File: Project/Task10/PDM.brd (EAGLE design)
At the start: 100 x 80 mm, 43 parts

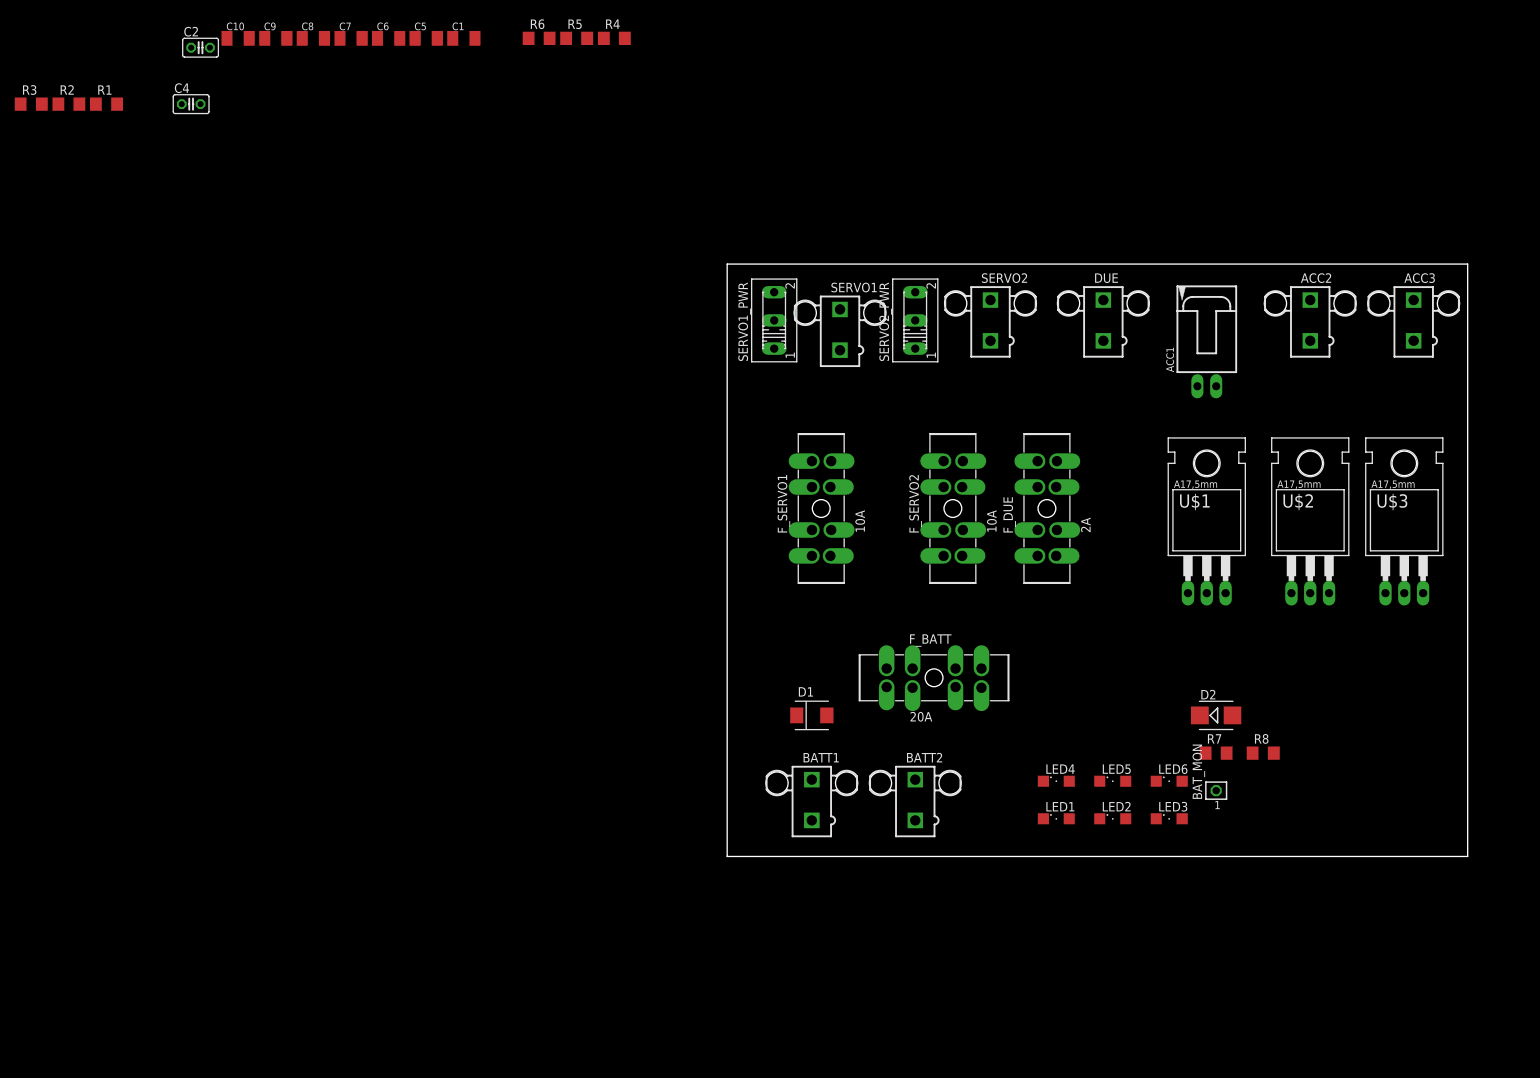
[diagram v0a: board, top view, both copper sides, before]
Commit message: Datahseet for XT60 for battery connector added
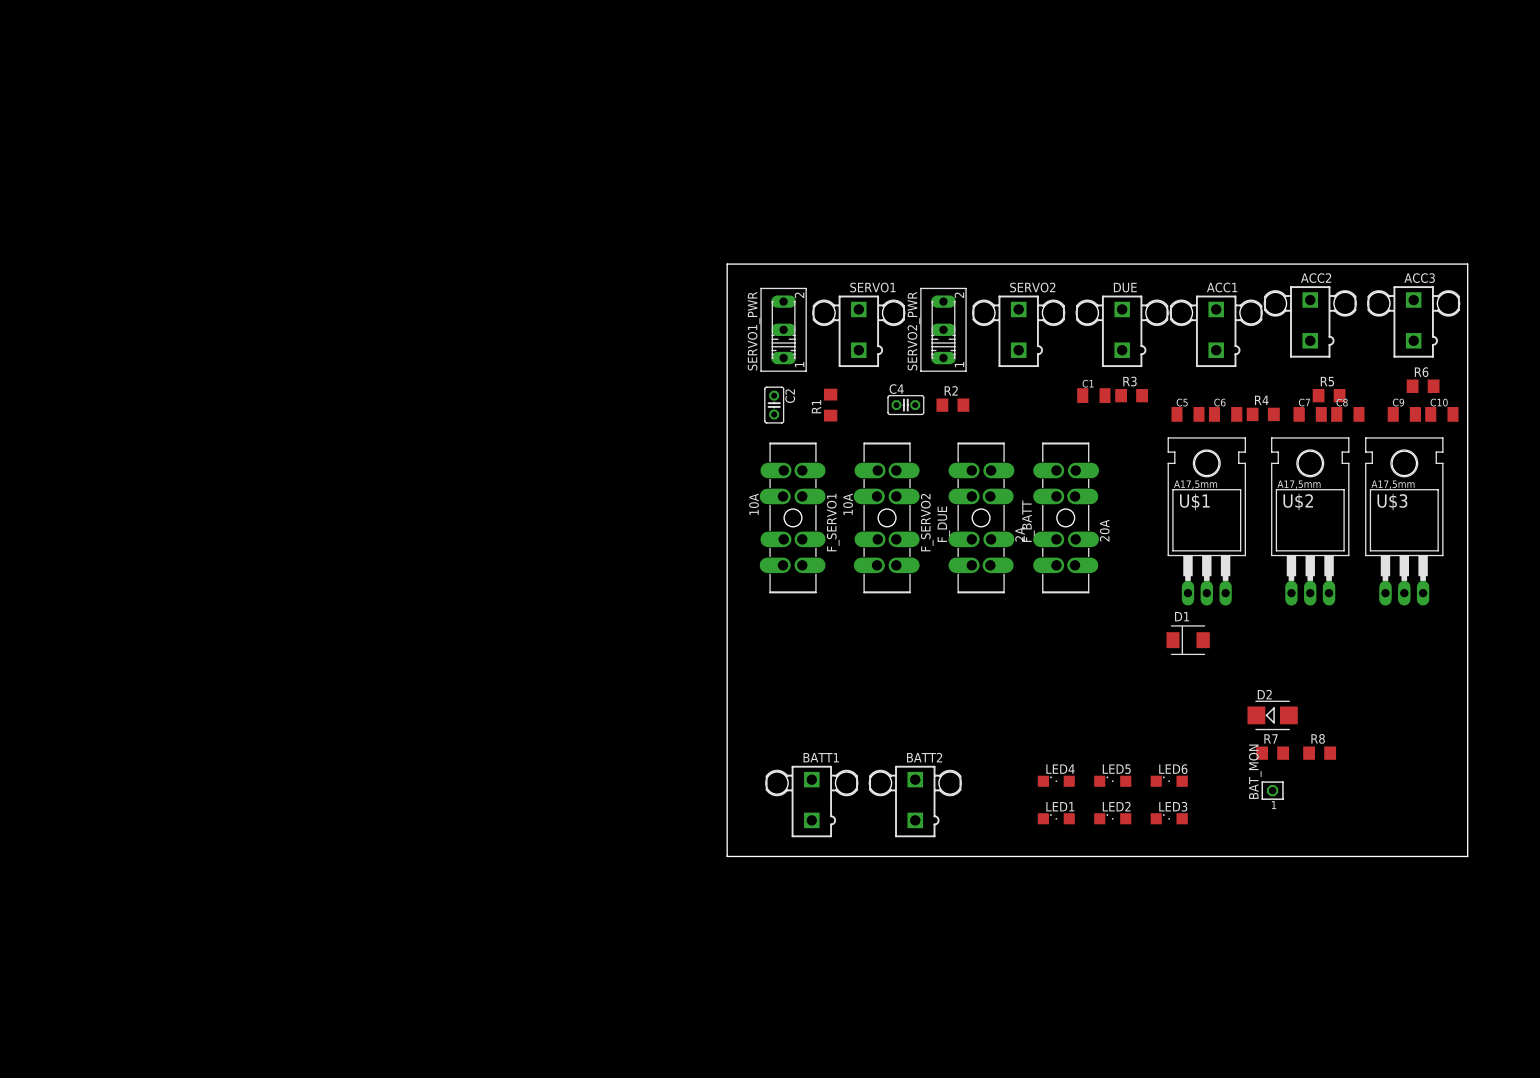
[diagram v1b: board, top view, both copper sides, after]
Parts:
- ACC1: value C-GRID-02-70553 -> (none); device con-molex:70553-02 -> con-molex:5566-2
- moved C10 170.3 mm to (96.5, 59.7)
- moved C9 160.6 mm to (91.4, 59.7)
- moved R3 153.7 mm to (54.6, 62.2)
- moved C8 148.6 mm to (83.8, 59.7)
- moved C7 139.1 mm to (78.7, 59.7)
- moved R6 128.3 mm to (94.0, 63.5)
- moved R2 126.1 mm to (30.5, 61.0)
- moved C6 123.9 mm to (67.3, 59.7)
- moved C5 114.7 mm to (62.2, 59.7)
- moved R5 112.5 mm to (81.3, 62.2)
- moved R1 105.9 mm to (14.0, 61.0), turned to 90 degrees
- moved C4 104.7 mm to (24.1, 61.0)
- moved R4 101.3 mm to (72.4, 59.7)
- moved C1 97.8 mm to (49.5, 62.2)
- moved C2 91.3 mm to (6.35, 61.0), turned to 270 degrees
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
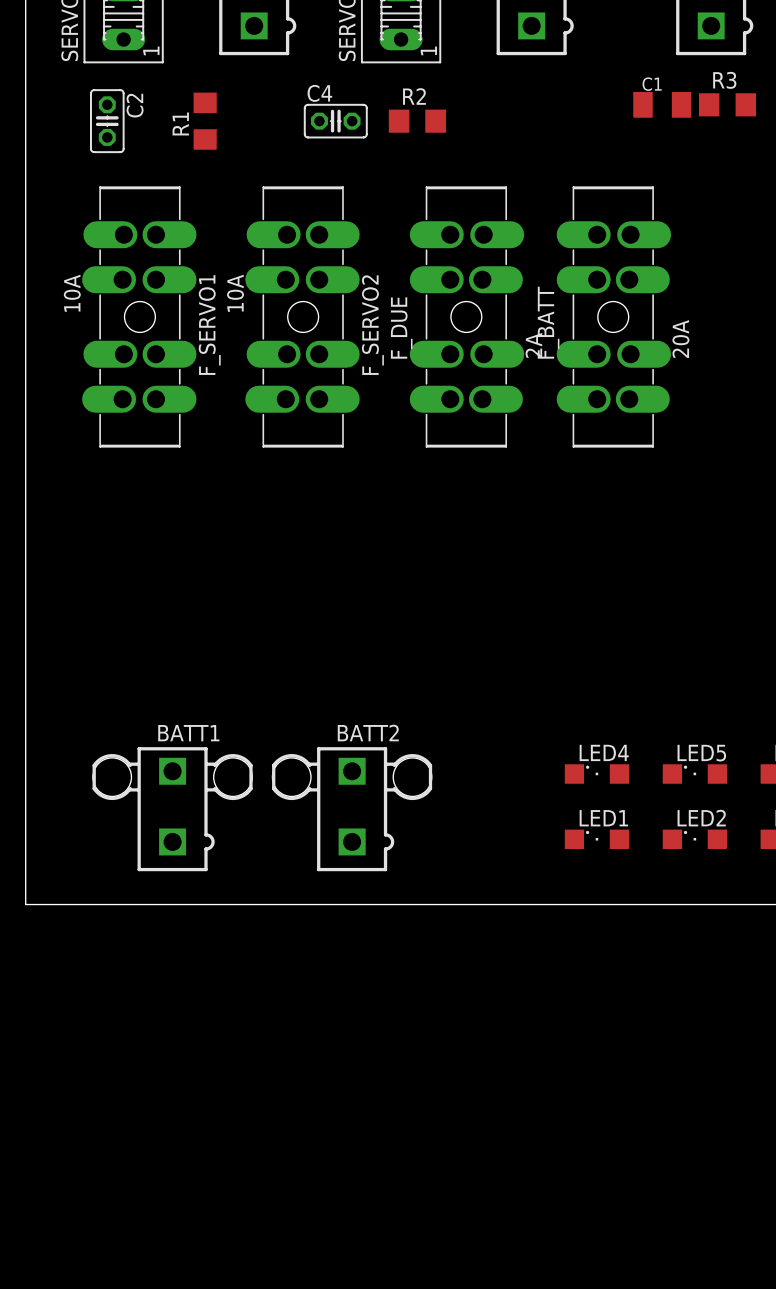
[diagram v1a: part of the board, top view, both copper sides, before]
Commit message: Fixed Capacitors and Schematic
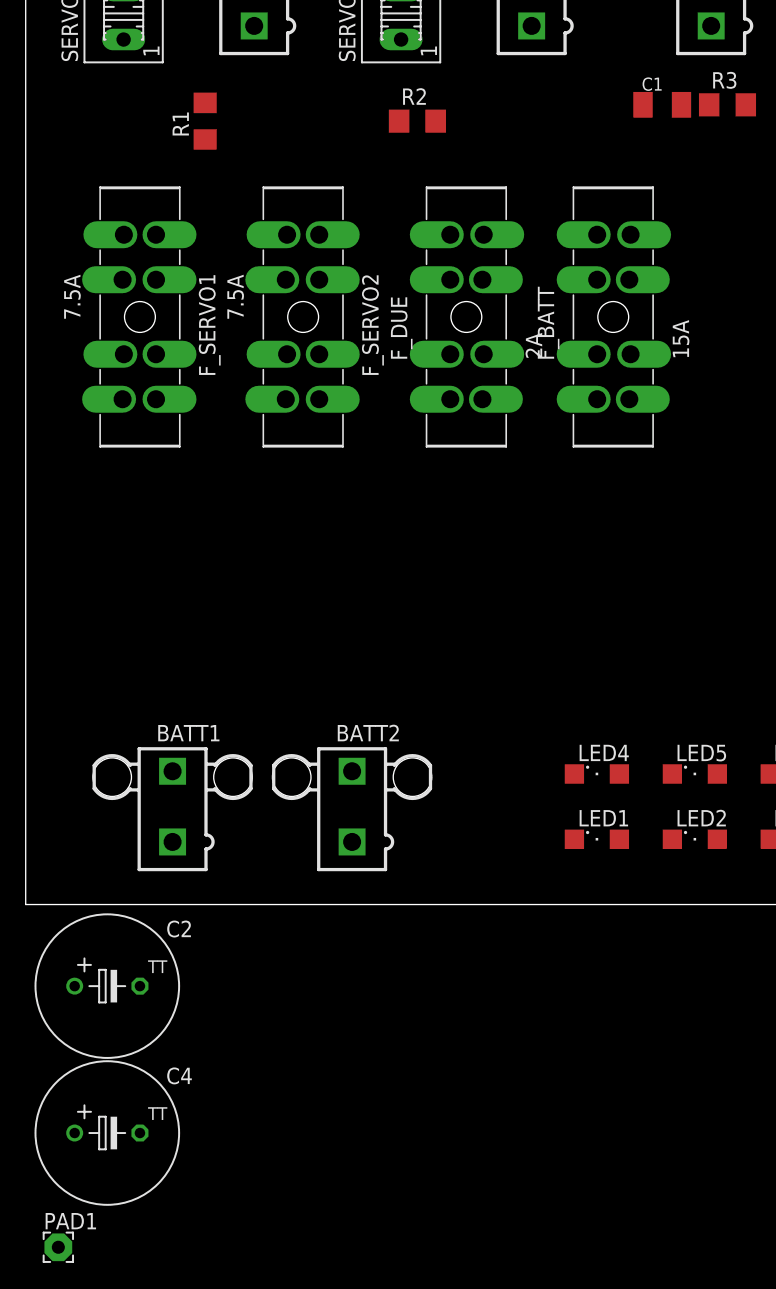
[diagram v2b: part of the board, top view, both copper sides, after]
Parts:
- added PAD1: (no value), wirepad:2,15/1,0
- C2: device TinyGadget(1):C025-025X050 -> rcl:TT5D11
- C4: value CAPACITORTH_CAP -> (none); device TinyGadget(1):C025-025X050 -> rcl:TT5D11
- F_BATT: value 20A -> 15A
- F_SERVO1, F_SERVO2: value 10A -> 7.5A
- moved C4 80.7 mm to (6.35, -17.8)
- moved C2 67.3 mm to (6.35, -6.35), turned to 0 degrees
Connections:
- net GND: now also C2.-, C4.-; no longer C2.2, C4.2
- net N$1: now also C4.+; no longer C4.1
- net N$15: now also C2.+; no longer C2.1
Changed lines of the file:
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@@
 <attribute name="OC_FARNELL" value="unknown" x="166.37" y="-81.28" size="1.778" layer="27" display="off"/>
 </element>
-<element name="C2" library="TinyGadget(1)" package="C025-025X050" value="" x="6.35" y="60.96" rot="R270"/>
-<element name="C4" library="TinyGadget(1)" package="C025-025X050" value="CAPACITORTH_CAP" x="24.13" y="60.96"/>
 <element name="ACC3" library="con-molex" package="5566-2" value="" x="92.71" y="72.39">
 <attribute name="OC_NEWARK" value="unknown" x="138.43" y="-19.05" size="1.778" layer="27" display="off"/>
@@
 <element name="U$2" library="MRSDTeamB" package="TO220H" value="MIC29150/29300/29500HORIZONTAL" x="78.74" y="41.91"/>
 <element name="U$3" library="MRSDTeamB" package="TO220H" value="MIC29150/29300/29500HORIZONTAL" x="91.44" y="41.91"/>
-<element name="F_BATT" library="MRSDTeamB" package="ATO" value="20A" x="45.72" y="45.72" rot="R90"/>
+<element name="F_BATT" library="MRSDTeamB" package="ATO" value="15A" x="45.72" y="45.72" rot="R90"/>
 <element name="F_DUE" library="MRSDTeamB" package="ATO" value="2A" x="34.29" y="45.72" rot="R90"/>
-<element name="F_SERVO1" library="MRSDTeamB" package="ATO" value="10A" x="8.89" y="45.72" rot="R270"/>
-<element name="F_SERVO2" library="MRSDTeamB" package="ATO" value="10A" x="21.59" y="45.72" rot="R270"/>
+<element name="F_SERVO1" library="MRSDTeamB" package="ATO" value="7.5A" x="8.89" y="45.72" rot="R270"/>
+<element name="F_SERVO2" library="MRSDTeamB" package="ATO" value="7.5A" x="21.59" y="45.72" rot="R270"/>
 <element name="ACC1" library="con-molex" package="5566-2" value="" x="66.04" y="71.12">
 <attribute name="OC_NEWARK" value="unknown" x="66.04" y="71.12" size="1.778" layer="27" display="off"/>
@@
 <attribute name="OC_FARNELL" value="1822072" x="66.04" y="71.12" size="1.778" layer="27" display="off"/>
 </element>
+<element name="C2" library="rcl" package="TT5D11" value="" x="6.35" y="-6.35"/>
+<element name="C4" library="rcl" package="TT5D11" value="" x="6.35" y="-17.78"/>
+<element name="PAD1" library="wirepad" package="2,15/1,0" value="" x="2.54" y="-26.67"/>
 </elements>
 <signals>
@@
 <contactref element="LED2" pad="C"/>
 <contactref element="LED5" pad="C"/>
-<contactref element="C4" pad="2"/>
 <contactref element="SERVO1" pad="2"/>
-<contactref element="LED6" pad="C"/>
-<contactref element="C2" pad="2"/>
 <contactref element="C10" pad="2"/>
 <contactref element="C9" pad="2"/>
@@
 <contactref element="SERVO2" pad="2"/>
 <contactref element="ACC1" pad="2"/>
+<contactref element="C2" pad="-"/>
+<contactref element="C4" pad="-"/>
+<contactref element="LED6" pad="C"/>
 <wire x1="78.74" y1="75.14" x2="92.71" y2="75.14" width="0" layer="19" extent="1-1"/>
-<wire x1="92.94" y1="59.69" x2="92.71" y2="75.14" width="0" layer="19" extent="1-1"/>
+<wire x1="66.04" y1="73.87" x2="78.74" y2="75.14" width="0" layer="19" extent="1-1"/>
+<wire x1="53.34" y1="73.87" x2="66.04" y2="73.87" width="0" layer="19" extent="1-1"/>
+<wire x1="51.03" y1="62.23" x2="53.34" y2="73.87" width="0" layer="19" extent="1-1"/>
+<wire x1="63.73" y1="59.69" x2="51.03" y2="62.23" width="0" layer="19" extent="1-1"/>
+<wire x1="68.81" y1="59.69" x2="63.73" y2="59.69" width="0" layer="19" extent="1-1"/>
+<wire x1="80.24" y1="59.69" x2="68.81" y2="59.69" width="0" layer="19" extent="1-1"/>
+<wire x1="85.32" y1="59.69" x2="80.24" y2="59.69" width="0" layer="19" extent="1-1"/>
+<wire x1="92.94" y1="59.69" x2="85.32" y2="59.69" width="0" layer="19" extent="1-1"/>
 <wire x1="98.02" y1="59.69" x2="92.94" y2="59.69" width="0" layer="19" extent="1-1"/>
-<wire x1="85.32" y1="59.69" x2="92.94" y2="59.69" width="0" layer="19" extent="1-1"/>
-<wire x1="80.24" y1="59.69" x2="85.32" y2="59.69" width="0" layer="19" extent="1-1"/>
-<wire x1="68.81" y1="59.69" x2="80.24" y2="59.69" width="0" layer="19" extent="1-1"/>
-<wire x1="63.73" y1="59.69" x2="68.81" y2="59.69" width="0" layer="19" extent="1-1"/>
-<wire x1="51.03" y1="62.23" x2="63.73" y2="59.69" width="0" layer="19" extent="1-1"/>
-<wire x1="53.34" y1="73.87" x2="51.03" y2="62.23" width="0" layer="19" extent="1-1"/>
 <wire x1="39.37" y1="73.87" x2="53.34" y2="73.87" width="0" layer="19" extent="1-1"/>
-<wire x1="25.4" y1="60.96" x2="39.37" y2="73.87" width="0" layer="19" extent="1-1"/>
-<wire x1="17.78" y1="73.87" x2="25.4" y2="60.96" width="0" layer="19" extent="1-1"/>
-<wire x1="6.35" y1="59.69" x2="17.78" y2="73.87" width="0" layer="19" extent="1-1"/>
+<wire x1="17.78" y1="73.87" x2="39.37" y2="73.87" width="0" layer="19" extent="1-1"/>
 <wire x1="64.77" y1="35.56" x2="63.73" y2="59.69" width="0" layer="19" extent="1-1"/>
 <wire x1="64.27" y1="29.21" x2="64.77" y2="35.56" width="0" layer="19" extent="1-1"/>
@@
 <wire x1="25.4" y1="10.37" x2="42.7" y2="10.16" width="0" layer="19" extent="1-1"/>
 <wire x1="11.43" y1="10.37" x2="25.4" y2="10.37" width="0" layer="19" extent="1-1"/>
-<wire x1="66.04" y1="73.87" x2="11.43" y2="10.37" width="0" layer="19" extent="1-1"/>
+<wire x1="8.89" y1="-6.35" x2="11.43" y2="10.37" width="0" layer="19" extent="1-1"/>
+<wire x1="8.89" y1="-17.78" x2="8.89" y2="-6.35" width="0" layer="19" extent="1-1"/>
 </signal>
 <signal name="N$1">
-<contactref element="C4" pad="1"/>
 <contactref element="R2" pad="2"/>
 <contactref element="SERVO2" pad="1"/>
-<contactref element="F_SERVO2" pad="B1"/>
 <contactref element="F_SERVO2" pad="B2"/>
 <contactref element="F_SERVO2" pad="B3"/>
 <contactref element="F_SERVO2" pad="B4"/>
-<wire x1="22.84" y1="39.32" x2="39.37" y2="68.37" width="0" layer="19" extent="1-1"/>
+<contactref element="F_SERVO2" pad="B1"/>
+<contactref element="C4" pad="+"/>
+<wire x1="31.902" y1="60.96" x2="39.37" y2="68.37" width="0" layer="19" extent="1-1"/>
+<wire x1="22.84" y1="42.82" x2="31.902" y2="60.96" width="0" layer="19" extent="1-1"/>
+<wire x1="20.34" y1="42.82" x2="22.84" y2="42.82" width="0" layer="19" extent="1-1"/>
+<wire x1="22.84" y1="39.32" x2="22.84" y2="42.82" width="0" layer="19" extent="1-1"/>
 <wire x1="20.24" y1="39.32" x2="22.84" y2="39.32" width="0" layer="19" extent="1-1"/>
-<wire x1="22.84" y1="42.82" x2="22.84" y2="39.32" width="0" layer="19" extent="1-1"/>
-<wire x1="20.34" y1="42.82" x2="22.84" y2="42.82" width="0" layer="19" extent="1-1"/>
-<wire x1="22.86" y1="60.96" x2="22.84" y2="42.82" width="0" layer="19" extent="1-1"/>
-<wire x1="31.902" y1="60.96" x2="22.86" y2="60.96" width="0" layer="19" extent="1-1"/>
+<wire x1="3.81" y1="-17.78" x2="20.24" y2="39.32" width="0" layer="19" extent="1-1"/>
 </signal>
 <signal name="N$15">
 <contactref element="SERVO1" pad="1"/>
-<contactref element="C2" pad="1"/>
 <contactref element="R1" pad="2"/>
-<contactref element="F_SERVO1" pad="B1"/>
 <contactref element="F_SERVO1" pad="B2"/>
 <contactref element="F_SERVO1" pad="B3"/>
 <contactref element="F_SERVO1" pad="B4"/>
+<contactref element="F_SERVO1" pad="B1"/>
+<contactref element="C2" pad="+"/>
+<wire x1="13.97" y1="62.382" x2="17.78" y2="68.37" width="0" layer="19" extent="1-1"/>
+<wire x1="10.14" y1="42.82" x2="13.97" y2="62.382" width="0" layer="19" extent="1-1"/>
+<wire x1="7.64" y1="42.82" x2="10.14" y2="42.82" width="0" layer="19" extent="1-1"/>
+<wire x1="10.14" y1="39.32" x2="10.14" y2="42.82" width="0" layer="19" extent="1-1"/>
 <wire x1="7.54" y1="39.32" x2="10.14" y2="39.32" width="0" layer="19" extent="1-1"/>
-<wire x1="10.14" y1="42.82" x2="10.14" y2="39.32" width="0" layer="19" extent="1-1"/>
-<wire x1="7.64" y1="42.82" x2="10.14" y2="42.82" width="0" layer="19" extent="1-1"/>
-<wire x1="6.35" y1="62.23" x2="10.14" y2="42.82" width="0" layer="19" extent="1-1"/>
-<wire x1="13.97" y1="62.382" x2="6.35" y2="62.23" width="0" layer="19" extent="1-1"/>
-<wire x1="17.78" y1="68.37" x2="13.97" y2="62.382" width="0" layer="19" extent="1-1"/>
+<wire x1="3.81" y1="-6.35" x2="7.54" y2="39.32" width="0" layer="19" extent="1-1"/>
 </signal>
 <signal name="N$18">
